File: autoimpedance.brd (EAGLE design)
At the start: 32.1 x 50.8 mm, 43 parts, among them IC1 AD5933, IC2 LM234, IC3 AD5245, Q1 DMG2307L-7

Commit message: Remove built for imp logo'
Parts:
- removed JP8: FIDUCIALUFIDUCIAL, SparkFun:MICRO-FIDUCIAL

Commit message: Add Gerber files and .cam
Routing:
- net VIN: track 27.9 -> 29.5 mm
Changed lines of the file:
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@@
 <layer number="1" name="Top" color="4" fill="1" visible="no" active="yes"/>
 <layer number="2" name="Route2" color="11" fill="1" visible="no" active="yes"/>
-<layer number="3" name="Route3" color="8" fill="1" visible="no" active="yes"/>
+<layer number="3" name="Route3" color="8" fill="1" visible="yes" active="yes"/>
 <layer number="4" name="Route4" color="1" fill="4" visible="no" active="no"/>
 <layer number="5" name="Route5" color="4" fill="4" visible="no" active="no"/>
@@
 <layer number="15" name="Route15" color="4" fill="6" visible="no" active="no"/>
 <layer number="16" name="Bottom" color="1" fill="1" visible="no" active="yes"/>
-<layer number="17" name="Pads" color="2" fill="1" visible="no" active="yes"/>
-<layer number="18" name="Vias" color="2" fill="1" visible="no" active="yes"/>
+<layer number="17" name="Pads" color="2" fill="1" visible="yes" active="yes"/>
+<layer number="18" name="Vias" color="2" fill="1" visible="yes" active="yes"/>
 <layer number="19" name="Unrouted" color="15" fill="1" visible="no" active="yes"/>
 <layer number="20" name="Dimension" color="15" fill="1" visible="no" active="yes"/>
-<layer number="21" name="tPlace" color="3" fill="1" visible="no" active="yes"/>
+<layer number="21" name="tPlace" color="3" fill="1" visible="yes" active="yes"/>
 <layer number="22" name="bPlace" color="5" fill="1" visible="yes" active="yes"/>
 <layer number="23" name="tOrigins" color="15" fill="1" visible="no" active="yes"/>
 <layer number="24" name="bOrigins" color="15" fill="1" visible="no" active="yes"/>
-<layer number="25" name="tNames" color="3" fill="1" visible="no" active="yes"/>
+<layer number="25" name="tNames" color="3" fill="1" visible="yes" active="yes"/>
 <layer number="26" name="bNames" color="5" fill="1" visible="yes" active="yes"/>
-<layer number="27" name="tValues" color="3" fill="1" visible="no" active="yes"/>
+<layer number="27" name="tValues" color="3" fill="1" visible="yes" active="yes"/>
 <layer number="28" name="bValues" color="5" fill="1" visible="yes" active="yes"/>
 <layer number="29" name="tStop" color="7" fill="1" visible="no" active="yes"/>
@@
 <wire x1="10.3632" y1="13.2381" x2="10.3632" y2="12.3444" width="0.254" layer="1"/>
 <wire x1="10.3632" y1="12.3444" x2="10.5156" y2="12.192" width="0.254" layer="1"/>
-<wire x1="10.5156" y1="12.192" x2="11.8872" y2="12.192" width="0.254" layer="1"/>
-<wire x1="11.8872" y1="12.192" x2="12.3444" y2="12.6492" width="0.254" layer="1"/>
-<wire x1="12.3444" y1="12.6492" x2="13.4112" y2="12.6492" width="0.254" layer="1"/>
+<wire x1="10.5156" y1="12.192" x2="11.811" y2="12.192" width="0.254" layer="1"/>
+<wire x1="11.811" y1="12.192" x2="12.2682" y2="12.6492" width="0.254" layer="1"/>
+<wire x1="12.2682" y1="12.6492" x2="13.4112" y2="12.6492" width="0.254" layer="1"/>
 <wire x1="13.4112" y1="12.6492" x2="13.716" y2="12.954" width="0.254" layer="1"/>
 <wire x1="5.7404" y1="13.5636" x2="1.524" y2="13.5636" width="0.8128" layer="1"/>
@@
 <wire x1="15.24" y1="14.478" x2="13.513" y2="14.478" width="0.254" layer="1"/>
 <wire x1="13.513" y1="14.478" x2="13.5128" y2="15.3164" width="0.254" layer="1"/>
-<wire x1="1.5646" y1="5.6032" x2="7.1272" y2="8.956" width="0.6096" layer="3"/>
-<wire x1="7.1272" y1="8.956" x2="12.8016" y2="14.6304" width="0.6096" layer="3"/>
-<wire x1="12.8016" y1="14.6304" x2="12.8016" y2="16.764" width="0.6096" layer="3"/>
+<wire x1="1.5646" y1="5.6032" x2="1.5646" y2="8.3464" width="0.6096" layer="3"/>
+<wire x1="1.5646" y1="8.3464" x2="7.6962" y2="14.478" width="0.6096" layer="3"/>
+<wire x1="7.6962" y1="14.478" x2="11.8872" y2="14.478" width="0.6096" layer="3"/>
+<wire x1="11.8872" y1="14.478" x2="12.8016" y2="15.24" width="0.6096" layer="3"/>
+<wire x1="12.8016" y1="15.24" x2="12.8016" y2="16.764" width="0.6096" layer="3"/>
 <wire x1="13.5128" y1="15.3164" x2="13.5128" y2="16.51" width="0.3048" layer="1"/>
 <wire x1="13.5128" y1="16.51" x2="13.2588" y2="16.764" width="0.3048" layer="1"/>
@@
 <wire x1="3.3932" y1="20.8788" x2="4.7244" y2="20.8788" width="0.4064" layer="16"/>
 <via x="4.7244" y="20.8788" extent="1-16" drill="0.381"/>
-<wire x1="12.192" y1="11.7348" x2="9.7536" y2="11.7348" width="0.4064" layer="1"/>
-<wire x1="9.7536" y1="11.7348" x2="9.4488" y2="11.43" width="0.4064" layer="1"/>
+<wire x1="12.1158" y1="11.6586" x2="9.6774" y2="11.6586" width="0.4064" layer="1"/>
+<wire x1="9.6774" y1="11.6586" x2="9.4488" y2="11.43" width="0.4064" layer="1"/>
 <wire x1="9.4488" y1="11.43" x2="9.4488" y2="10.5211" width="0.4064" layer="1"/>
 <wire x1="9.4488" y1="10.5211" x2="9.4132" y2="10.6379" width="0.4064" layer="1"/>
-<wire x1="12.192" y1="11.7348" x2="12.4968" y2="12.0396" width="0.4064" layer="1"/>
-<wire x1="12.4968" y1="12.0396" x2="14.7828" y2="12.0396" width="0.4064" layer="1"/>
-<wire x1="14.7828" y1="12.0396" x2="14.9352" y2="12.0396" width="0.4064" layer="1"/>
+<wire x1="12.1158" y1="11.6586" x2="12.4968" y2="12.0396" width="0.4064" layer="1"/>
+<wire x1="12.4968" y1="12.0396" x2="14.859" y2="12.0396" width="0.4064" layer="1"/>
+<wire x1="14.859" y1="12.0396" x2="14.9352" y2="12.0396" width="0.4064" layer="1"/>
 <wire x1="14.9352" y1="12.0396" x2="15.6972" y2="11.2776" width="0.4064" layer="1"/>
 <wire x1="15.6972" y1="11.2776" x2="15.6972" y2="9.6012" width="0.4064" layer="1"/>
@@
 <wire x1="12.0396" y1="14.1732" x2="12.3444" y2="13.8684" width="0.254" layer="1"/>
 <wire x1="12.3444" y1="13.8684" x2="14.1732" y2="13.8684" width="0.254" layer="1"/>
-<wire x1="14.1732" y1="13.8684" x2="14.7828" y2="13.2588" width="0.254" layer="1"/>
-<wire x1="14.7828" y1="13.2588" x2="14.7828" y2="12.0396" width="0.254" layer="1"/>
+<wire x1="14.1732" y1="13.8684" x2="14.859" y2="13.1826" width="0.254" layer="1"/>
+<wire x1="14.859" y1="13.1826" x2="14.859" y2="12.0396" width="0.254" layer="1"/>
 <wire x1="10.6426" y1="15.3418" x2="10.414" y2="15.6464" width="0.254" layer="1"/>
 <wire x1="10.414" y1="15.6464" x2="10.414" y2="16.8656" width="0.254" layer="1"/>

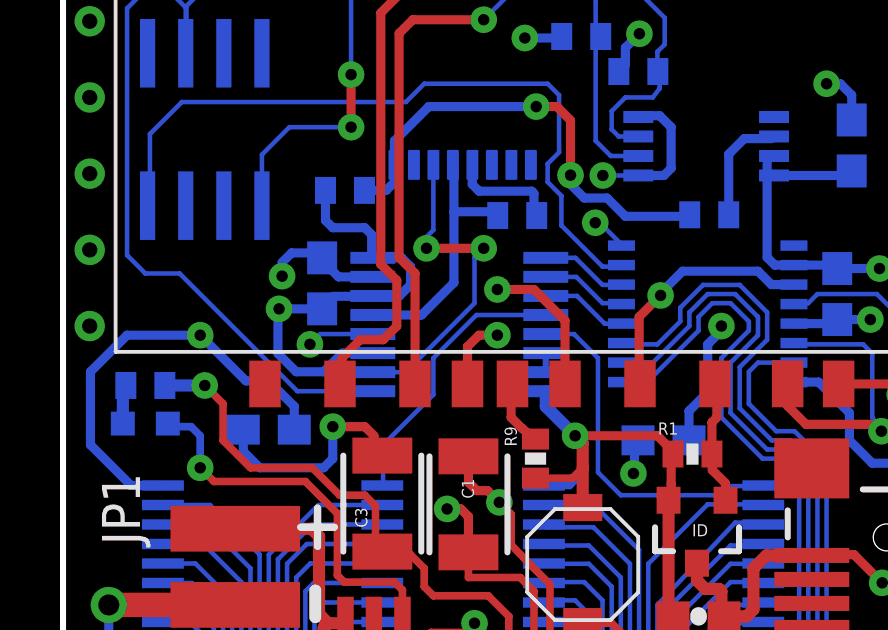
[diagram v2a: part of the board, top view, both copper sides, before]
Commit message: Fix incorrect VEE connection on 3x2 MUX
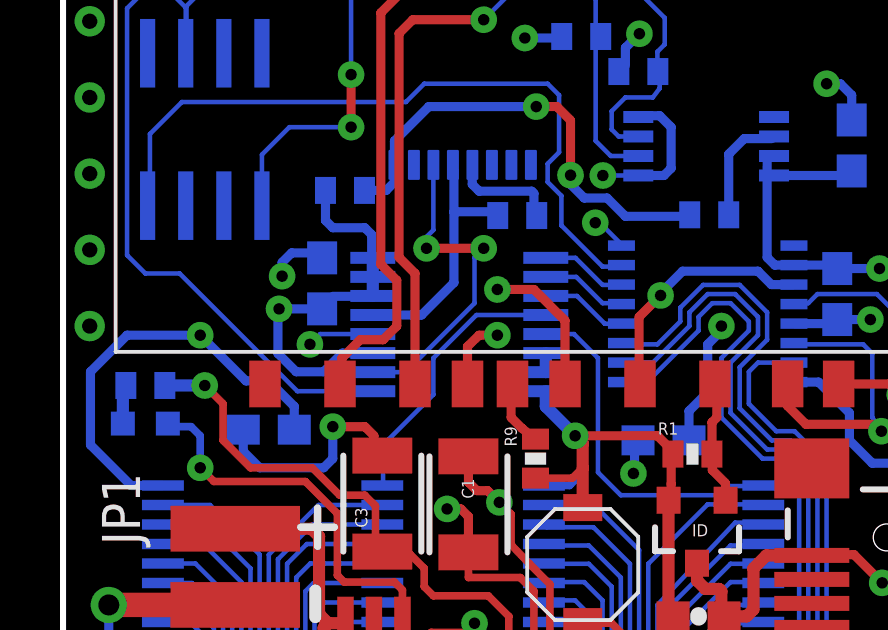
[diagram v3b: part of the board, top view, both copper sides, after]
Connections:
- net 3.3V: no longer MUX3X2.7
- net GND: now also MUX3X2.7
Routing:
- net GND: track 113.8 -> 111.7 mm
- net 3.3V: track 96.1 -> 94.4 mm
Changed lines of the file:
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@@
 <grid distance="0.003" unitdist="inch" unit="inch" style="lines" multiple="1" display="yes" altdistance="0.005" altunitdist="inch" altunit="inch"/>
 <layers>
-<layer number="1" name="Top" color="4" fill="1" visible="no" active="yes"/>
+<layer number="1" name="Top" color="8" fill="1" visible="no" active="yes"/>
 <layer number="2" name="Route2" color="11" fill="1" visible="no" active="yes"/>
-<layer number="3" name="Route3" color="8" fill="1" visible="yes" active="yes"/>
+<layer number="3" name="Route3" color="8" fill="1" visible="no" active="yes"/>
 <layer number="4" name="Route4" color="1" fill="4" visible="no" active="no"/>
 <layer number="5" name="Route5" color="4" fill="4" visible="no" active="no"/>
@@
 <layer number="14" name="Route14" color="1" fill="6" visible="no" active="no"/>
 <layer number="15" name="Route15" color="4" fill="6" visible="no" active="no"/>
-<layer number="16" name="Bottom" color="1" fill="1" visible="no" active="yes"/>
+<layer number="16" name="Bottom" color="8" fill="1" visible="yes" active="yes"/>
 <layer number="17" name="Pads" color="2" fill="1" visible="yes" active="yes"/>
 <layer number="18" name="Vias" color="2" fill="1" visible="yes" active="yes"/>
-<layer number="19" name="Unrouted" color="15" fill="1" visible="no" active="yes"/>
-<layer number="20" name="Dimension" color="15" fill="1" visible="no" active="yes"/>
-<layer number="21" name="tPlace" color="3" fill="1" visible="yes" active="yes"/>
+<layer number="19" name="Unrouted" color="15" fill="1" visible="yes" active="yes"/>
+<layer number="20" name="Dimension" color="15" fill="1" visible="yes" active="yes"/>
+<layer number="21" name="tPlace" color="3" fill="1" visible="no" active="yes"/>
 <layer number="22" name="bPlace" color="5" fill="1" visible="yes" active="yes"/>
 <layer number="23" name="tOrigins" color="15" fill="1" visible="no" active="yes"/>
-<layer number="24" name="bOrigins" color="15" fill="1" visible="no" active="yes"/>
-<layer number="25" name="tNames" color="3" fill="1" visible="yes" active="yes"/>
+<layer number="24" name="bOrigins" color="15" fill="1" visible="yes" active="yes"/>
+<layer number="25" name="tNames" color="3" fill="1" visible="no" active="yes"/>
 <layer number="26" name="bNames" color="5" fill="1" visible="yes" active="yes"/>
-<layer number="27" name="tValues" color="3" fill="1" visible="yes" active="yes"/>
-<layer number="28" name="bValues" color="5" fill="1" visible="yes" active="yes"/>
+<layer number="27" name="tValues" color="3" fill="1" visible="no" active="yes"/>
+<layer number="28" name="bValues" color="5" fill="1" visible="no" active="yes"/>
 <layer number="29" name="tStop" color="7" fill="1" visible="no" active="yes"/>
 <layer number="30" name="bStop" color="7" fill="1" visible="no" active="yes"/>
@@
 <wire x1="10.3251" y1="21.9583" x2="9.3091" y2="21.9583" width="0.3048" layer="16"/>
 <wire x1="9.3091" y1="21.9583" x2="8.6868" y2="21.336" width="0.3048" layer="16"/>
-<wire x1="10.3251" y1="25.1333" x2="11.2903" y2="25.1333" width="0.3048" layer="16"/>
-<wire x1="11.2903" y1="25.1333" x2="11.5824" y2="24.8412" width="0.3048" layer="16"/>
-<wire x1="11.5824" y1="24.8412" x2="11.5824" y2="24.2316" width="0.3048" layer="16"/>
-<wire x1="11.5824" y1="24.2316" x2="11.2014" y2="23.8506" width="0.3048" layer="16"/>
-<wire x1="11.2014" y1="23.8506" x2="10.3124" y2="23.8506" width="0.3048" layer="16"/>
-<wire x1="10.3124" y1="23.8506" x2="10.3251" y2="23.8633" width="0.1524" layer="16"/>
 <wire x1="18.6134" y1="25.5414" x2="18.5928" y2="25.6032" width="0.1524" layer="16"/>
 <wire x1="18.5928" y1="25.6032" x2="17.8926" y2="26.3034" width="0.1524" layer="16"/>
@@
 <wire x1="19.2024" y1="9.9568" x2="19.2024" y2="10.3092" width="0.254" layer="1"/>
 <wire x1="19.2024" y1="10.3092" x2="19.1872" y2="10.3244" width="0.254" layer="1"/>
+<contactref element="MUX3X2" pad="7"/>
+<wire x1="10.3251" y1="24.4983" x2="10.3251" y2="25.1333" width="0.4064" layer="16"/>
 <wire x1="31.115" y1="40.64" x2="31.1912" y2="40.64" width="0" layer="19" extent="1-1"/>
 <wire x1="18.2372" y1="11.0744" x2="18.2118" y2="10.5156" width="0" layer="19" extent="1-1"/>
+<wire x1="10.3251" y1="24.4983" x2="10.3251" y2="23.8633" width="0.4064" layer="16"/>
 </signal>
 <signal name="3.3V">
@@
 <contactref element="CLK" pad="7"/>
 <contactref element="CLK" pad="8"/>
-<contactref element="MUX3X2" pad="7"/>
 <contactref element="MUX3X2" pad="16"/>
 <contactref element="MUX16A" pad="24"/>
@@
 <wire x1="12.3444" y1="36.7284" x2="12.3444" y2="36.0333" width="0.3048" layer="16"/>
 <wire x1="12.3444" y1="36.0333" x2="12.3456" y2="36.0321" width="0.1524" layer="16"/>
-<wire x1="10.3251" y1="24.4983" x2="9.1821" y2="24.4983" width="0.3048" layer="16"/>
-<wire x1="9.1821" y1="24.4983" x2="8.8392" y2="24.8412" width="0.3048" layer="16"/>
 <via x="7.3016" y="24.5228" extent="1-16" drill="0.381"/>
 <wire x1="18.527" y1="31.3436" x2="18.7452" y2="31.5468" width="0.1524" layer="16"/>
@@
 <wire x1="7.62" y1="25.2984" x2="8.47" y2="25.2984" width="0.3048" layer="16"/>
 <wire x1="8.47" y1="25.2984" x2="8.636" y2="25.1324" width="0.254" layer="16"/>
-<wire x1="8.8392" y1="24.8412" x2="8.8392" y2="24.9292" width="0.254" layer="16"/>
+<wire x1="8.8392" y1="24.8412" x2="8.8392" y2="24.9292" width="0" layer="19" extent="1-16"/>
 <wire x1="8.8392" y1="24.9292" x2="8.636" y2="25.1324" width="0.254" layer="16"/>
 <wire x1="23.4696" y1="27.9532" x2="23.471" y2="28.5642" width="0.3048" layer="16"/>
@@
 <wire x1="3.7728" y1="37.5276" x2="3.7338" y2="37.5666" width="0.3048" layer="16"/>
 <wire x1="3.7338" y1="37.5666" x2="3.7338" y2="38.481" width="0.3048" layer="16"/>
+<wire x1="9.1821" y1="24.4983" x2="8.8392" y2="24.8412" width="0" layer="19" extent="1-16"/>
 </signal>
 <signal name="ID">
@@
 <contactref element="MUX3X2" pad="14"/>
 <contactref element="MUX3X2" pad="15"/>
-<wire x1="16.0909" y1="21.9583" x2="16.0909" y2="21.3233" width="0.2032" layer="16"/>
+<wire x1="16.0909" y1="21.3233" x2="16.0909" y2="21.9583" width="0.4064" layer="16"/>
 </signal>
 <signal name="T9">

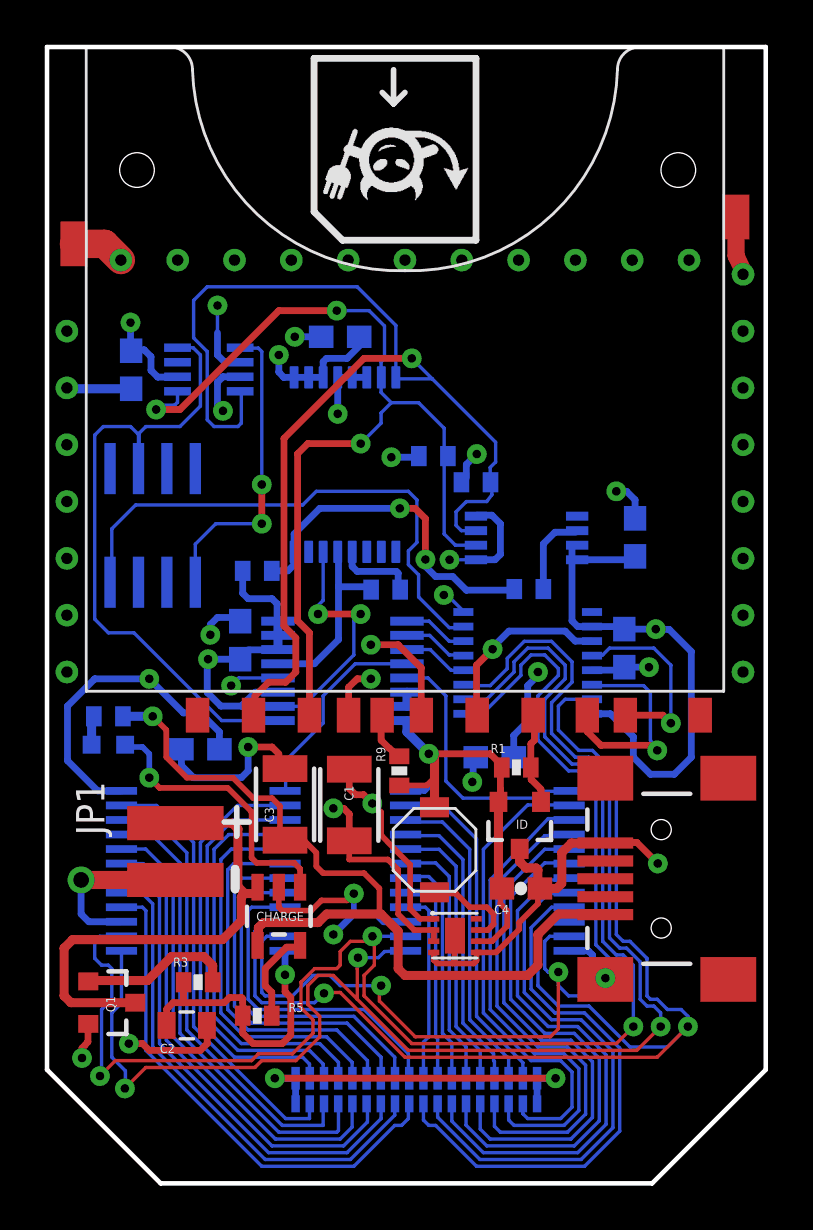
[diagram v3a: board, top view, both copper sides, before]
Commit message: Switch to i2c89 instead of i2c12
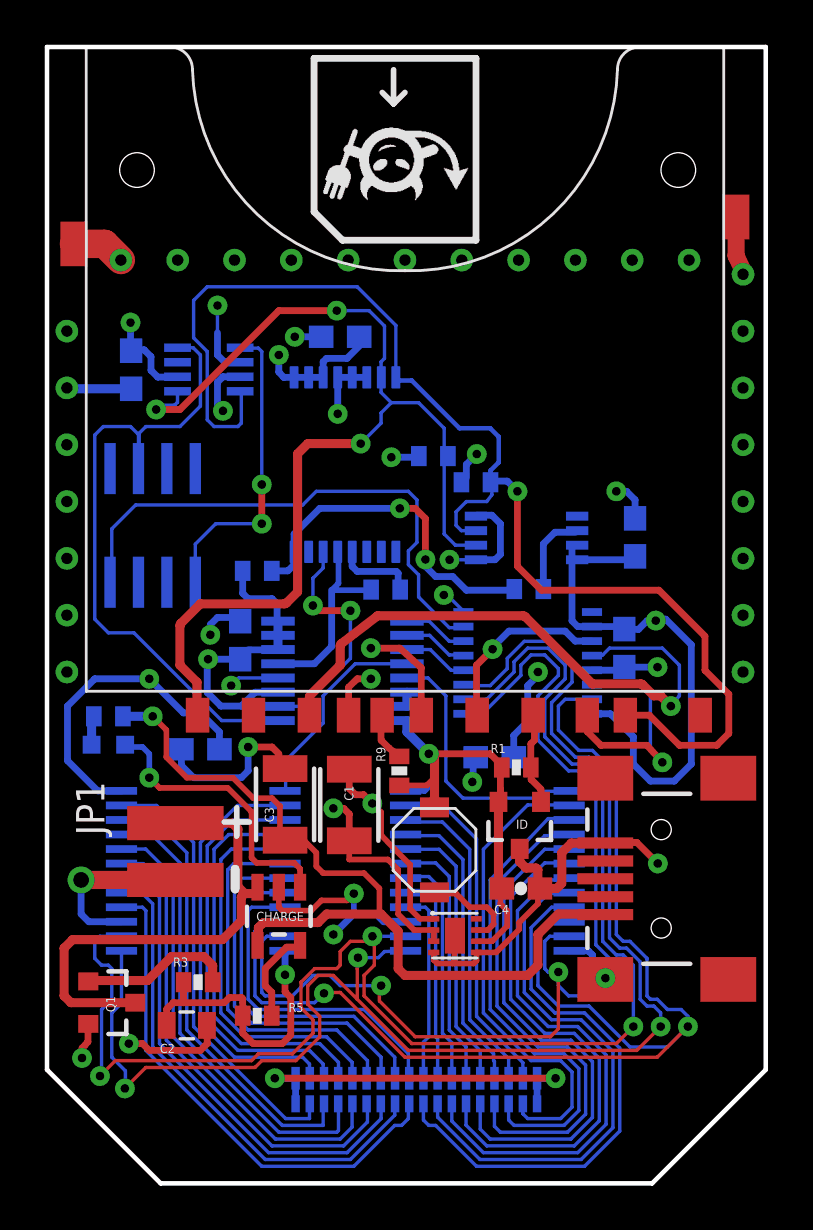
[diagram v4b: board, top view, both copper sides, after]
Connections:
- removed net PIN9: SD.9
- new net PIN1: SD.1
- net RCK: now also SD.2; no longer SD.8
- net SCL: now also SD.8; no longer SD.1
- net SDA: now also SD.9; no longer SD.2
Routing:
- net RCK: track 8.76 -> 27.0 mm
- net SDA: track 44.3 -> 48.8 mm
- net SCL: track 55.5 -> 57.7 mm
- net SER: track 9.65 -> 10.8 mm
- net 3.3V: track 94.4 -> 95.5 mm
